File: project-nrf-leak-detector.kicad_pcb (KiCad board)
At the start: 2 copper layers, 51.3 x 36.8 mm, 16 parts, among them J1 Conn_02x05_Odd_Even, J2 Water Probe, Q1 Q_NMOS_GSD, U1 MS88SF3_NRF52840

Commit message: Add info on silkscreen
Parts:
- added Ref**: Val**, project-nrf-leak-detector_hardware:Firma, B.Cu at (43.2, 60.7)
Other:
- board text added: "20 nov. 2022"
- board text added: "v1.0.0"

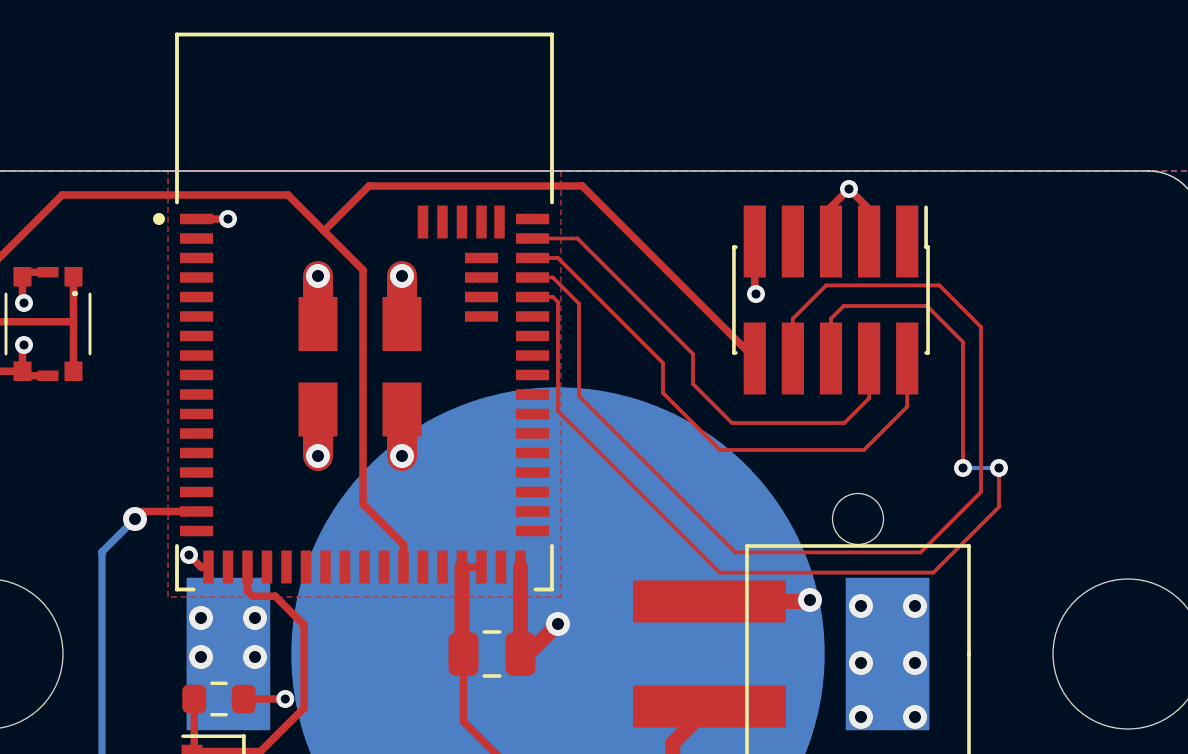
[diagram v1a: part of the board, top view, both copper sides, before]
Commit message: Change RX pin to P0.24
To avoid crossing over TX.
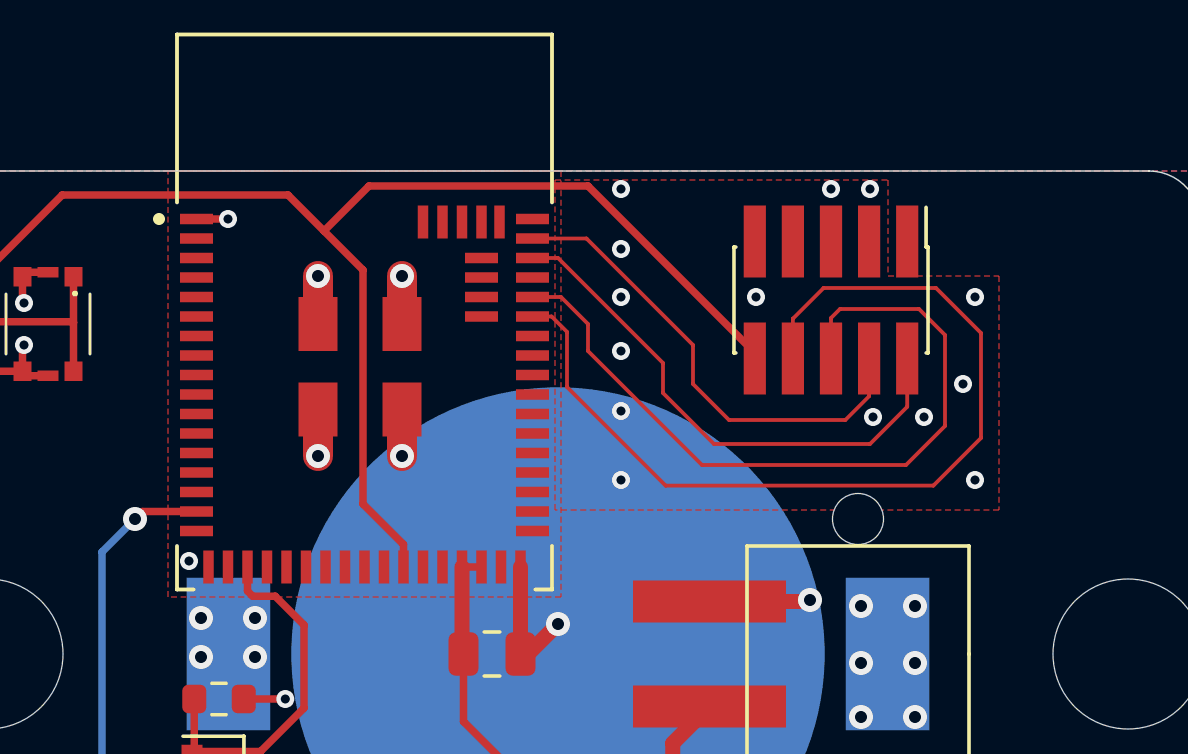
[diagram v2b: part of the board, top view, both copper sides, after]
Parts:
- removed Ref**: Val**, project-nrf-leak-detector_hardware:Firma
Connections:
- U1 pad 46: Net-(U1-Pad46) -> /RX
- U1 pad 48: /RX -> Net-(U1-Pad48)
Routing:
- net /TX: track 35.5 -> 25.8 mm, vias 2 -> 0
- net GND: track 29.9 -> 23.3 mm, vias 14 -> 26
- net /RX: track 35.5 -> 31.2 mm

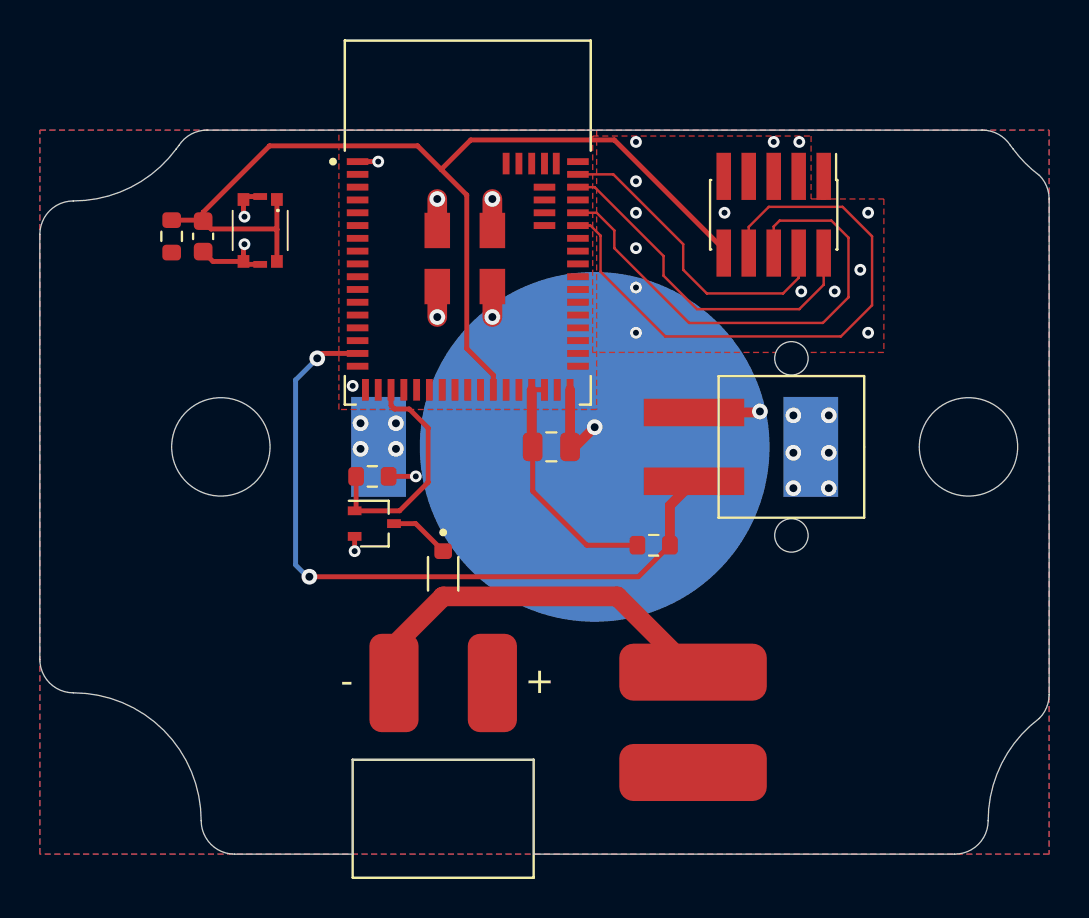
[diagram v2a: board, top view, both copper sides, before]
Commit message: Add a cap on the probe signal
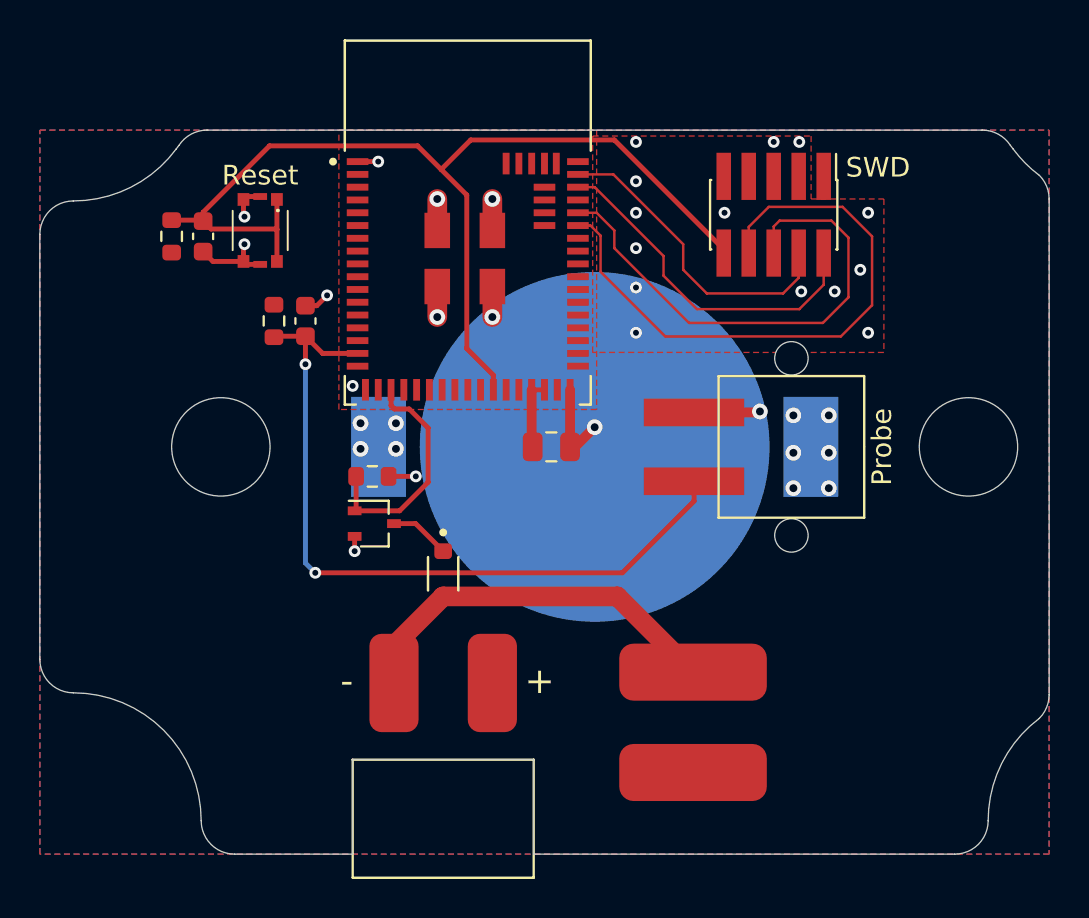
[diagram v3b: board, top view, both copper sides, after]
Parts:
- added C3: 100nF, Capacitor_SMD:C_0603_1608Metric, F.Cu at (43.5, 44.3)
- added Ref**: Val**, project-nrf-leak-detector_hardware:Firma, B.Cu at (42.9, 60.9)
- moved R3 22.4 mm to (41.9, 44.3), turned to 270 degrees
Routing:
- net VDD: track 12.3 -> 3.57 mm
- net /WATER_PROBE: track 36.8 -> 38.6 mm
- net GND: track 23.3 -> 24.6 mm, vias 26 -> 27
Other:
- board text added: "Probe"
- board text added: "Reset"
- board text added: "SWD"

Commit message: Add the turtle
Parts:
- removed the Ref** at (42.9, 60.9)
- added Ref**: Val**, project-nrf-leak-detector_hardware:turtle-01.inverted, B.Cu at (71.2, 61.2)
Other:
- board text added: "13 dec. 2022"
- board text removed: "20 nov. 2022"

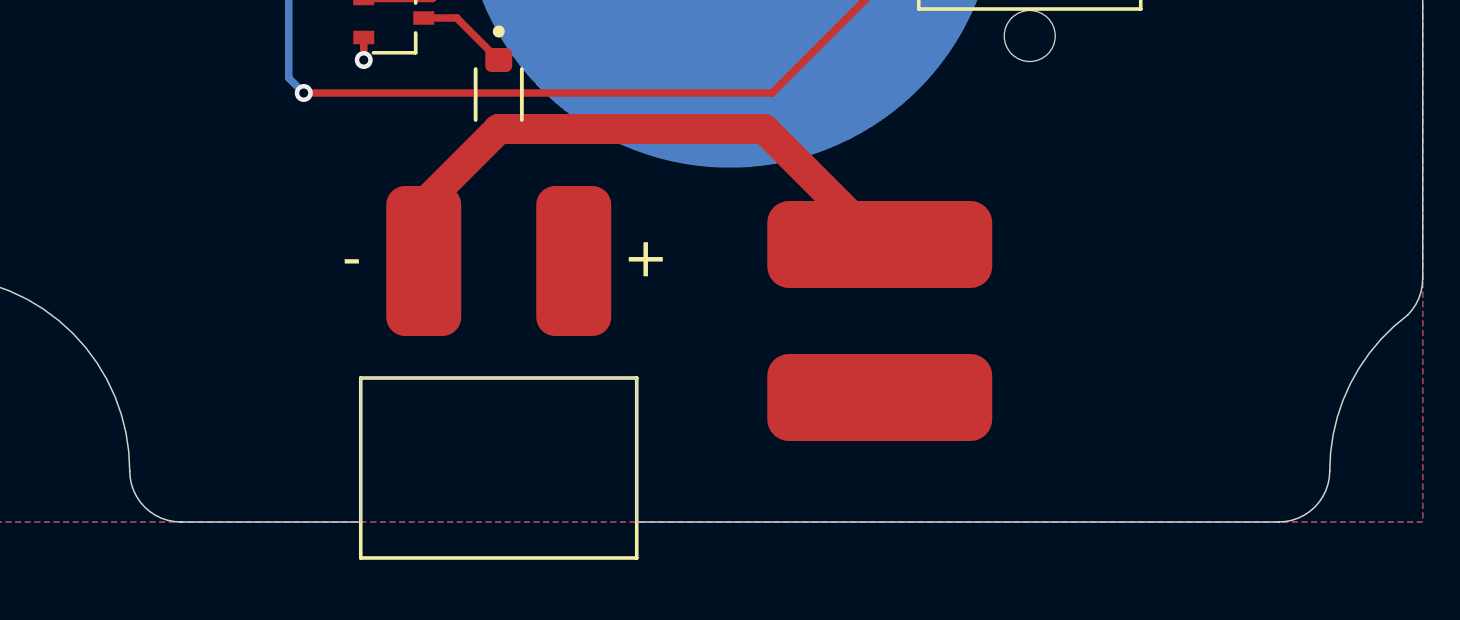
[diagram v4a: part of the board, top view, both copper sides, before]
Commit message: Change the buzzer slot size and position
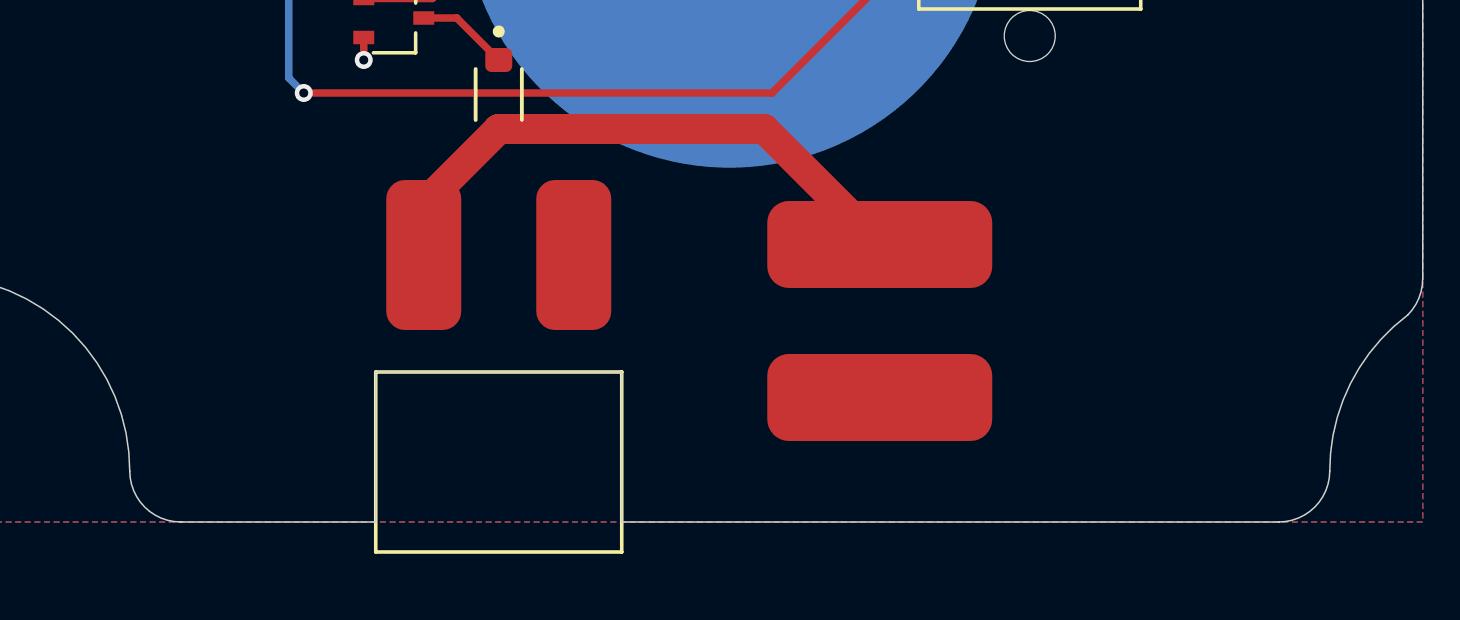
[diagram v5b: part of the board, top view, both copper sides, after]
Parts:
- moved LS1 0.20 mm to (50.5, 62.5)
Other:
- outline, holes or cut-outs redrawn
- board text added: "15 dec. 2022"
- board text removed: "13 dec. 2022"
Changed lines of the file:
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@@
   (page A4)
   (layers
-    (0 F.Cu signal hide)
+    (0 F.Cu signal)
     (31 B.Cu signal hide)
     (32 B.Adhes user hide)
@@
   )
   (setup
-    (last_trace_width 0.25)
+    (last_trace_width 0.5)
     (user_trace_width 0.127)
     (user_trace_width 0.5)
@@
       (outputformat 1)
       (mirror false)
-      (drillshape 1)
+      (drillshape 0)
       (scaleselection 1)
-      (outputdirectory ""))
+      (outputdirectory "gerbers/"))
   )
   (net 0 "")
@@
     (add_net "Net-(U1-Pad9)")
     (add_net VDD)
+  )
+  (module PKM13EPYH4000-A0:SPKR_PKM13EPYH4000-A0_SMD (layer F.Cu)
+    (at 50.5 62.5)
+    (fp_text reference LS1 (at 0 -4.2) (layer F.Fab)
+      (effects (font (size 1 1) (thickness 0.15)))
+    )
+    (fp_text value PKM13EPYH4000-A0 (at 10.005 7.755) (layer F.Fab)
+      (effects (font (size 1 1) (thickness 0.15)))
+    )
+    (fp_text user + (at 4.9 -0.1) (layer F.Fab)
+      (effects (font (size 1.32 1.32) (thickness 0.15)))
+    )
+    (fp_line (start -4.4 10.2) (end -4.4 3.6) (layer F.CrtYd) (width 0.05))
+    (fp_line (start 4.4 10.2) (end -4.4 10.2) (layer F.CrtYd) (width 0.05))
+    (fp_line (start 4.4 3.6) (end 4.4 10.2) (layer F.CrtYd) (width 0.05))
+    (fp_line (start -4.4 3.6) (end 4.4 3.6) (layer F.CrtYd) (width 0.05))
+    (fp_line (start -4.1 9.9) (end -4.1 3.9) (layer F.Fab) (width 0.12))
+    (fp_line (start 4.1 9.9) (end -4.1 9.9) (layer F.Fab) (width 0.12))
+    (fp_line (start 4.1 3.9) (end 4.1 9.9) (layer F.Fab) (width 0.12))
+    (fp_line (start -4.1 3.9) (end 4.1 3.9) (layer F.Fab) (width 0.12))
+    (fp_line (start 4.1 3.9) (end 4.1 9.9) (layer F.SilkS) (width 0.12))
+    (fp_line (start -4.1 3.9) (end -4.1 9.9) (layer F.SilkS) (width 0.12))
+    (fp_line (start 4.1 9.9) (end -4.1 9.9) (layer F.SilkS) (width 0.12))
+    (fp_line (start -4.1 3.9) (end 4.1 3.9) (layer F.SilkS) (width 0.12))
+    (pad P smd roundrect (at 2.5 0) (size 2.5 5) (layers F.Cu F.Paste F.Mask) (roundrect_rratio 0.25)
+      (net 2 VDD))
+    (pad N smd roundrect (at -2.5 0) (size 2.5 5) (layers F.Cu F.Paste F.Mask) (roundrect_rratio 0.25)
+      (net 5 "Net-(D1-Pad2)"))
+    (model ${KIPRJMOD}/kicad-library/PKM13EPYH4000-A0/PKM13EPYH4000-A0.step
+      (offset (xyz 0 -3 4.78))
+      (scale (xyz 1 1 1))
+      (rotate (xyz -180 0 0))
+    )
   )
   (module project-nrf-leak-detector_hardware:turtle-01.inverted locked (layer B.Cu)
@@
     )
   )
-  (module PKM13EPYH4000-A0:SPKR_PKM13EPYH4000-A0_SMD (layer F.Cu)
-    (at 50.5 62.7)
-    (fp_text reference LS1 (at 0 -4.2) (layer F.Fab)
-      (effects (font (size 1 1) (thickness 0.15)))
-    )
-    (fp_text value PKM13EPYH4000-A0 (at 10.005 7.755) (layer F.Fab)
-      (effects (font (size 1 1) (thickness 0.15)))
-    )
-    (fp_line (start -4.6 3.9) (end 4.6 3.9) (layer F.SilkS) (width 0.12))
-    (fp_line (start 4.6 9.9) (end -4.6 9.9) (layer F.SilkS) (width 0.12))
-    (fp_line (start -4.6 3.9) (end -4.6 9.9) (layer F.SilkS) (width 0.12))
-    (fp_line (start 4.6 3.9) (end 4.6 9.9) (layer F.SilkS) (width 0.12))
-    (fp_line (start -4.6 3.9) (end 4.6 3.9) (layer F.Fab) (width 0.12))
-    (fp_line (start 4.6 3.9) (end 4.6 9.9) (layer F.Fab) (width 0.12))
-    (fp_line (start 4.6 9.9) (end -4.6 9.9) (layer F.Fab) (width 0.12))
-    (fp_line (start -4.6 9.9) (end -4.6 3.9) (layer F.Fab) (width 0.12))
-    (fp_line (start -4.9 3.6) (end 4.9 3.6) (layer F.CrtYd) (width 0.05))
-    (fp_line (start 4.9 3.6) (end 4.9 10.2) (layer F.CrtYd) (width 0.05))
-    (fp_line (start 4.9 10.2) (end -4.9 10.2) (layer F.CrtYd) (width 0.05))
-    (fp_line (start -4.9 10.2) (end -4.9 3.6) (layer F.CrtYd) (width 0.05))
-    (fp_text user + (at 4.9 -0.1) (layer F.SilkS)
-      (effects (font (size 1.32 1.32) (thickness 0.15)))
-    )
-    (fp_text user + (at 4.9 -0.1) (layer F.Fab)
-      (effects (font (size 1.32 1.32) (thickness 0.15)))
-    )
-    (fp_text user - (at -4.9 -0.1) (layer F.SilkS)
-      (effects (font (size 1.32 1.32) (thickness 0.15)))
-    )
-    (pad P smd roundrect (at 2.5 0) (size 2.5 5) (layers F.Cu F.Paste F.Mask) (roundrect_rratio 0.25)
-      (net 2 VDD))
-    (pad N smd roundrect (at -2.5 0) (size 2.5 5) (layers F.Cu F.Paste F.Mask) (roundrect_rratio 0.25)
-      (net 5 "Net-(D1-Pad2)"))
-    (model ${KIPRJMOD}/kicad-library/PKM13EPYH4000-A0/PKM13EPYH4000-A0.step
-      (offset (xyz 0 -3 4.3))
-      (scale (xyz 1 1 1))
-      (rotate (xyz -180 0 0))
-    )
-  )
   (module MS88SF3_NRF52840:MODULE_MS88SF3_NRF52840 (layer F.Cu)
     (at 51.75 39.3)
@@
     (effects (font (size 1 1) (thickness 0.15)) (justify mirror))
   )
-  (gr_text "13 dec. 2022" (at 31.7 61.7 270) (layer B.SilkS)
+  (gr_text "15 dec. 2022" (at 31.7 61.7 270) (layer B.SilkS)
     (effects (font (size 1 1) (thickness 0.15)) (justify left mirror))
   )
-  (gr_line (start 76.5 71.4) (end 55.1 71.4) (layer Edge.Cuts) (width 0.05))
-  (gr_line (start 55.1 66.6) (end 55.1 71.4) (layer Edge.Cuts) (width 0.05))
-  (gr_line (start 45.9 66.6) (end 55.1 66.6) (layer Edge.Cuts) (width 0.05))
-  (gr_line (start 45.9 71.4) (end 45.9 66.6) (layer Edge.Cuts) (width 0.05))
+  (gr_line (start 76.5 71.4) (end 54.6 71.4) (layer Edge.Cuts) (width 0.05))
+  (gr_line (start 54.6 66.4) (end 54.6 71.4) (layer Edge.Cuts) (width 0.05))
+  (gr_line (start 46.4 66.4) (end 54.6 66.4) (layer Edge.Cuts) (width 0.05))
+  (gr_line (start 46.4 71.4) (end 46.4 66.4) (layer Edge.Cuts) (width 0.05))
   (gr_arc (start 84.7 69.7) (end 80.8 64.5) (angle -53.13010235) (layer Edge.Cuts) (width 0.05))
   (gr_line (start 81.3 63.3) (end 81.3 38.1) (layer Edge.Cuts) (width 0.05))
@@
   (gr_arc (start 31.7 39.9) (end 31.7 38.2) (angle -90) (layer Edge.Cuts) (width 0.05))
   (gr_line (start 30 39.9) (end 30 61.5) (layer Edge.Cuts) (width 0.05))
-  (gr_line (start 45.9 71.4) (end 39.9 71.4) (layer Edge.Cuts) (width 0.05))
+  (gr_line (start 46.4 71.4) (end 39.9 71.4) (layer Edge.Cuts) (width 0.05))
   (via (at 60.3 44.9) (size 0.6) (drill 0.3) (layers F.Cu B.Cu) (net 1))
   (segment (start 63.25 48.95) (end 66.55 48.95) (width 0.5) (layer F.Cu) (net 1))
@@
   (via (at 60.3 40.6) (size 0.6) (drill 0.3) (layers F.Cu B.Cu) (net 1))
   (via (at 60.3 37.2) (size 0.6) (drill 0.3) (layers F.Cu B.Cu) (net 1))
-  (via (at 68.6 35.2) (size 0.6) (drill 0.3) (layers F.Cu B.Cu) (net 1))
   (via (at 67.3 35.2) (size 0.6) (drill 0.3) (layers F.Cu B.Cu) (net 1))
   (via (at 60.3 35.2) (size 0.6) (drill 0.3) (layers F.Cu B.Cu) (net 1))
@@
   (segment (start 43.5 43.525) (end 44.075 43.525) (width 0.25) (layer F.Cu) (net 1))
   (segment (start 44.075 43.525) (end 44.6 43) (width 0.25) (layer F.Cu) (net 1))
+  (via (at 68.6 35.2) (size 0.6) (drill 0.3) (layers F.Cu B.Cu) (net 1))
   (via (at 70.1 51) (size 0.8) (drill 0.4) (layers F.Cu B.Cu) (net 2))
   (via (at 68.3 51) (size 0.8) (drill 0.4) (layers F.Cu B.Cu) (net 2))
@@
   (segment (start 49.1 54.6) (end 50.5 56) (width 0.25) (layer F.Cu) (net 4))
   (segment (start 48 54.6) (end 49.1 54.6) (width 0.25) (layer F.Cu) (net 4))
-  (segment (start 48 60.8) (end 50.5 58.3) (width 1) (layer F.Cu) (net 5))
-  (segment (start 48 62.7) (end 48 60.8) (width 1) (layer F.Cu) (net 5))
   (segment (start 59.35 58.3) (end 63.2 62.15) (width 1) (layer F.Cu) (net 5))
   (segment (start 50.5 58.3) (end 59.35 58.3) (width 1) (layer F.Cu) (net 5))
+  (segment (start 48 60.8) (end 50.5 58.3) (width 1) (layer F.Cu) (net 5))
+  (segment (start 48 62.5) (end 48 60.8) (width 1) (layer F.Cu) (net 5))
   (segment (start 66.03 39.523) (end 66.03 40.85) (width 0.127) (layer F.Cu) (net 6))
   (segment (start 70.8 38.5) (end 67.053 38.5) (width 0.127) (layer F.Cu) (net 6))
